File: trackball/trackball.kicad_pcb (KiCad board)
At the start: 2 copper layers, 15 x 13.1 mm, 13 parts, among them P8 CONN_7, U1 BU52012HFV-TR, U2 BU52012HFV-TR, U3 BU52012HFV-TR, U4 BU52012HFV-TR

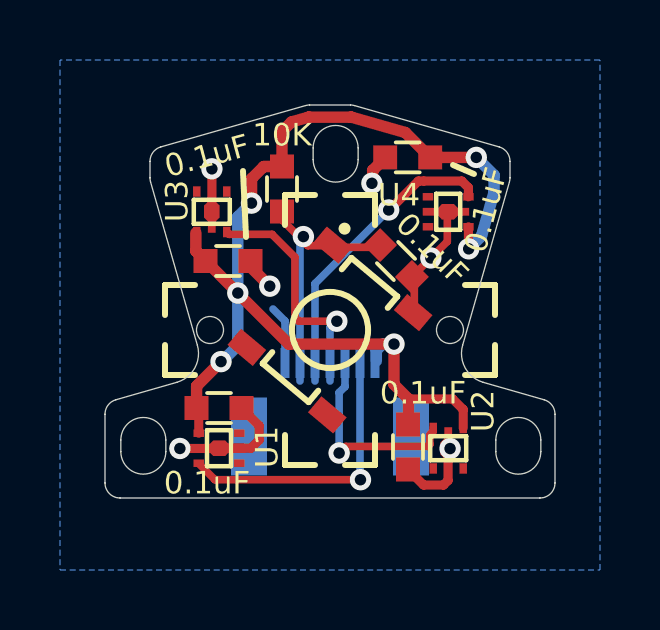
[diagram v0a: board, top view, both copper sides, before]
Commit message: Resolve 1 DRC error. 2 to go.
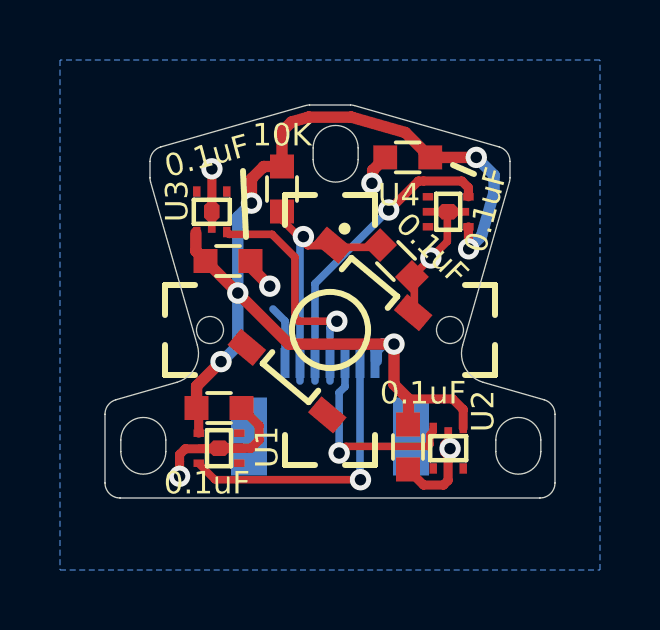
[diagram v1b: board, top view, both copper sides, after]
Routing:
- net GND: track 17.3 -> 18.1 mm
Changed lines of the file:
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@@
     (thickness 1.6)
     (drawings 43)
-    (tracks 128)
+    (tracks 131)
     (zones 0)
     (modules 13)
@@
     (effects (font (size 0.75 0.75) (thickness 0.15)) (justify mirror))
   )
-  (via (at 194.9958 153.9494) (size 0.7112) (drill 0.381) (layers F.Cu B.Cu) (net 1))
   (segment (start 202.810749 148.310749) (end 202.73033 148.23033) (width 0.254) (layer F.Cu) (net 1))
   (segment (start 202.810749 149.664124) (end 202.810749 148.310749) (width 0.254) (layer F.Cu) (net 1))
@@
   (segment (start 197.11 153.94) (end 196.0974 153.94) (width 0.3048) (layer F.Cu) (net 1))
   (segment (start 196.0974 153.94) (end 196.088 153.9306) (width 0.3048) (layer F.Cu) (net 1))
-  (segment (start 196.2906 153.9494) (end 196.3 153.94) (width 0.3048) (layer F.Cu) (net 1))
-  (segment (start 194.9958 153.9494) (end 196.2906 153.9494) (width 0.3048) (layer F.Cu) (net 1))
   (segment (start 197.6374 153.1874) (end 197.05 152.6) (width 0.3048) (layer F.Cu) (net 1))
   (segment (start 197.6374 153.67) (end 197.6374 153.1874) (width 0.3048) (layer F.Cu) (net 1))
@@
   (segment (start 201.8404 144.26) (end 201.422 144.6784) (width 0.381) (layer F.Cu) (net 1))
   (via (at 204.002044 153.951866) (size 0.7112) (drill 0.381) (layers F.Cu B.Cu) (net 1))
+  (via (at 194.986061 154.876501) (size 0.7112) (drill 0.381) (layers F.Cu B.Cu) (net 1))
+  (segment (start 196.3 153.94) (end 196.280601 153.959399) (width 0.3048) (layer F.Cu) (net 1))
+  (segment (start 196.280601 153.959399) (end 195.178044 153.959399) (width 0.3048) (layer F.Cu) (net 1))
+  (segment (start 195.178044 153.959399) (end 194.986061 154.151382) (width 0.3048) (layer F.Cu) (net 1))
+  (segment (start 194.986061 154.373607) (end 194.986061 154.876501) (width 0.3048) (layer F.Cu) (net 1))
+  (segment (start 194.986061 154.151382) (end 194.986061 154.373607) (width 0.3048) (layer F.Cu) (net 1))
   (segment (start 200.390425 147.2438) (end 200.335876 147.189251) (width 0.254) (layer F.Cu) (net 2))
   (segment (start 201.66967 147.16967) (end 201.59554 147.2438) (width 0.254) (layer F.Cu) (net 2))

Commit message: Move top edge upward by 0.3 mm. Resolve DRC issues.
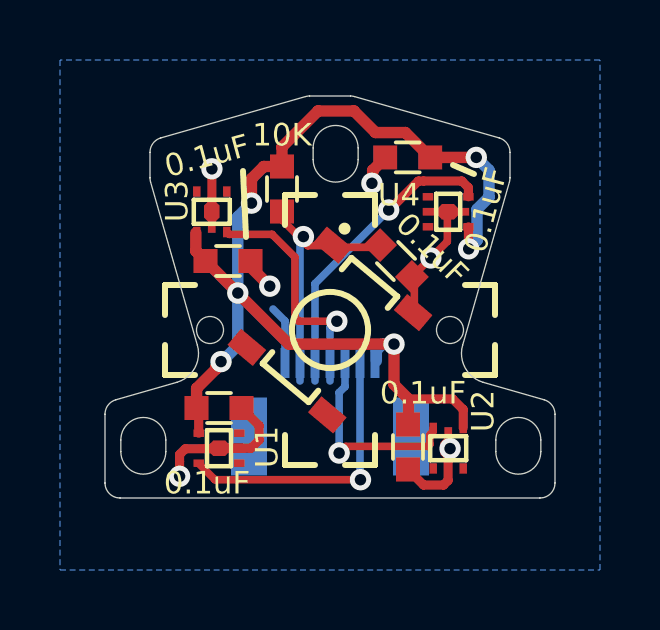
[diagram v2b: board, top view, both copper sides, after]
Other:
- board size 15 x 13.1 mm -> 15 x 13.4 mm
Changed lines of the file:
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@@
     (thickness 1.6)
     (drawings 43)
-    (tracks 131)
+    (tracks 132)
     (zones 0)
     (modules 13)
@@
   )
   (setup
-    (last_trace_width 0.2032)
+    (last_trace_width 0.381)
     (user_trace_width 0.2032)
     (user_trace_width 0.254)
@@
   (gr_circle (center 203.94 153.94) (end 203.99 153.94) (layer Eco2.User) (width 0.1))
   (gr_circle (center 196.06 146.06) (end 196.11 146.06) (layer Eco2.User) (width 0.1))
-  (gr_arc (start 199.320057 143.000091) (end 199.32003 142.499997) (angle -15.6) (layer Edge.Cuts) (width 0.01))
-  (gr_arc (start 200.679943 143.000091) (end 200.817329 142.519238) (angle -15.7) (layer Edge.Cuts) (width 0.01))
+  (gr_arc (start 199.320057 142.700091) (end 199.32003 142.199997) (angle -15.6) (layer Edge.Cuts) (width 0.01))
+  (gr_arc (start 200.679943 142.700091) (end 200.817329 142.219238) (angle -15.7) (layer Edge.Cuts) (width 0.01))
   (gr_arc (start 193.000061 155.099935) (end 192.5 155.100003) (angle -89.9) (layer Edge.Cuts) (width 0.01))
-  (gr_arc (start 194.500041 144.377192) (end 194.36264 143.89639) (angle -74) (layer Edge.Cuts) (width 0.01))
-  (gr_arc (start 205.499959 144.377192) (end 206 144.377148) (angle -74) (layer Edge.Cuts) (width 0.01))
+  (gr_arc (start 194.500041 144.077192) (end 194.36264 143.59639) (angle -74) (layer Edge.Cuts) (width 0.01))
+  (gr_arc (start 205.499959 144.077192) (end 206 144.077148) (angle -74) (layer Edge.Cuts) (width 0.01))
   (gr_arc (start 206.999958 152.806915) (end 207.5 152.806897) (angle -74) (layer Edge.Cuts) (width 0.01))
   (gr_arc (start 206.999932 155.099935) (end 207 155.600003) (angle -89.9) (layer Edge.Cuts) (width 0.01))
@@
   (gr_line (start 192.862183 152.32626) (end 194.893456 151.743802) (angle 90) (layer Edge.Cuts) (width 0.01))
   (gr_line (start 195.579079 150.506909) (end 194.019371 145.067548) (angle 90) (layer Edge.Cuts) (width 0.01))
-  (gr_line (start 200.817329 142.519238) (end 205.63736 143.89639) (angle 90) (layer Edge.Cuts) (width 0.01))
-  (gr_line (start 194.36264 143.89639) (end 199.182671 142.519238) (angle 90) (layer Edge.Cuts) (width 0.01))
-  (gr_line (start 194 144.92973) (end 194 144.377148) (angle 90) (layer Edge.Cuts) (width 0.01))
+  (gr_line (start 200.817329 142.219238) (end 205.63736 143.59639) (angle 90) (layer Edge.Cuts) (width 0.01))
+  (gr_line (start 194.36264 143.59639) (end 199.182671 142.219238) (angle 90) (layer Edge.Cuts) (width 0.01))
+  (gr_line (start 194 144.92973) (end 194 144.077148) (angle 90) (layer Edge.Cuts) (width 0.01))
   (gr_line (start 205.106544 151.743802) (end 207.137817 152.32626) (angle 90) (layer Edge.Cuts) (width 0.01))
-  (gr_line (start 199.32003 142.499997) (end 200.67997 142.499997) (angle 90) (layer Edge.Cuts) (width 0.01))
-  (gr_line (start 206 144.377148) (end 206 144.92973) (angle 90) (layer Edge.Cuts) (width 0.01))
+  (gr_line (start 199.32003 142.199997) (end 200.67997 142.199997) (angle 90) (layer Edge.Cuts) (width 0.01))
+  (gr_line (start 206 144.077148) (end 206 144.92973) (angle 90) (layer Edge.Cuts) (width 0.01))
   (gr_line (start 205.980629 145.067548) (end 204.420921 150.506909) (angle 90) (layer Edge.Cuts) (width 0.01))
   (gr_line (start 205.52729 154.054501) (end 205.52729 153.665707) (angle 90) (layer Edge.Cuts) (width 0.01))
@@
   (segment (start 195.5546 152.5016) (end 195.5546 152.6286) (width 0.381) (layer F.Cu) (net 4))
   (via (at 196.3674 151.0538) (size 0.7112) (drill 0.381) (layers F.Cu B.Cu) (net 4))
-  (segment (start 195.5546 152.5778) (end 195.5546 151.8666) (width 0.381) (layer F.Cu) (net 4))
-  (segment (start 195.5546 151.8666) (end 196.3674 151.0538) (width 0.381) (layer F.Cu) (net 4))
   (segment (start 196.9262 148.9964) (end 196.9262 150.5204) (width 0.381) (layer B.Cu) (net 4))
   (segment (start 196.9262 150.5204) (end 196.3928 151.0538) (width 0.381) (layer B.Cu) (net 4))
@@
   (via (at 204.8764 144.2466) (size 0.7112) (drill 0.381) (layers F.Cu B.Cu) (net 4))
   (segment (start 203.3404 144.2466) (end 204.8764 144.2466) (width 0.381) (layer F.Cu) (net 4))
-  (segment (start 200.734074 142.910116) (end 202.511853 143.418053) (width 0.381) (layer F.Cu) (net 4))
-  (segment (start 198.4 144.55) (end 198.4 143.3824) (width 0.381) (layer F.Cu) (net 4))
-  (segment (start 198.4 143.3824) (end 198.714828 143.067572) (width 0.381) (layer F.Cu) (net 4))
-  (segment (start 198.714828 143.067572) (end 199.267735 142.909598) (width 0.381) (layer F.Cu) (net 4))
-  (segment (start 199.267735 142.909598) (end 199.300098 142.905164) (width 0.381) (layer F.Cu) (net 4))
-  (segment (start 199.300098 142.905164) (end 200.699292 142.905164) (width 0.381) (layer F.Cu) (net 4))
-  (segment (start 202.511853 143.418053) (end 203.3404 144.2466) (width 0.381) (layer F.Cu) (net 4))
-  (segment (start 200.699292 142.905164) (end 200.734074 142.910116) (width 0.381) (layer F.Cu) (net 4))
-  (segment (start 205.468713 145.406312) (end 205.049815 146.867185) (width 0.381) (layer B.Cu) (net 4))
-  (segment (start 205.049815 146.867185) (end 204.6224 147.2946) (width 0.381) (layer B.Cu) (net 4))
-  (segment (start 205.468713 144.838913) (end 205.468713 145.406312) (width 0.381) (layer B.Cu) (net 4))
-  (segment (start 204.8764 144.2466) (end 205.468713 144.838913) (width 0.381) (layer B.Cu) (net 4))
   (via (at 204.6224 147.2946) (size 0.7112) (drill 0.381) (layers F.Cu B.Cu) (net 4))
   (segment (start 204.615 147.2872) (end 204.6224 147.2946) (width 0.3048) (layer F.Cu) (net 4))
@@
   (segment (start 195.625 152.675) (end 195.55 152.6) (width 0.3048) (layer F.Cu) (net 4))
   (segment (start 195.625 153.44) (end 195.625 152.675) (width 0.3048) (layer F.Cu) (net 4))
+  (segment (start 198.4 143.9) (end 198.4 144.5) (width 0.381) (layer F.Cu) (net 4))
+  (segment (start 199.6 142.7) (end 198.4 143.9) (width 0.381) (layer F.Cu) (net 4))
+  (segment (start 200.8 142.7) (end 199.6 142.7) (width 0.381) (layer F.Cu) (net 4))
+  (segment (start 203.3404 144.2466) (end 202.511853 143.418053) (width 0.381) (layer F.Cu) (net 4))
+  (segment (start 201.518053 143.418053) (end 200.8 142.7) (width 0.381) (layer F.Cu) (net 4))
+  (segment (start 202.511853 143.418053) (end 201.518053 143.418053) (width 0.381) (layer F.Cu) (net 4))
+  (segment (start 204.9 147.017) (end 204.6224 147.2946) (width 0.381) (layer B.Cu) (net 4))
+  (segment (start 204.9 145.975025) (end 204.9 147.017) (width 0.381) (layer B.Cu) (net 4))
+  (segment (start 205.3 145.575025) (end 204.9 145.975025) (width 0.381) (layer B.Cu) (net 4))
+  (segment (start 204.8764 144.2466) (end 205.3 144.6702) (width 0.381) (layer B.Cu) (net 4))
+  (segment (start 205.3 144.6702) (end 205.3 145.575025) (width 0.381) (layer B.Cu) (net 4))
+  (segment (start 196.2 151.2212) (end 196.3674 151.0538) (width 0.381) (layer F.Cu) (net 4))
+  (segment (start 196.2 151.3) (end 196.2 151.2212) (width 0.381) (layer F.Cu) (net 4))
+  (segment (start 195.5546 152.5778) (end 195.5546 151.9454) (width 0.381) (layer F.Cu) (net 4))
+  (segment (start 195.5546 151.9454) (end 196.2 151.3) (width 0.381) (layer F.Cu) (net 4))
   (via (at 200.3044 154.1018) (size 0.7112) (drill 0.381) (layers F.Cu B.Cu) (net 5))
   (segment (start 200.3044 152.083608) (end 200.3044 154.1018) (width 0.254) (layer B.Cu) (net 5))

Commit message: Move FFC connector upwards by 2 mm.
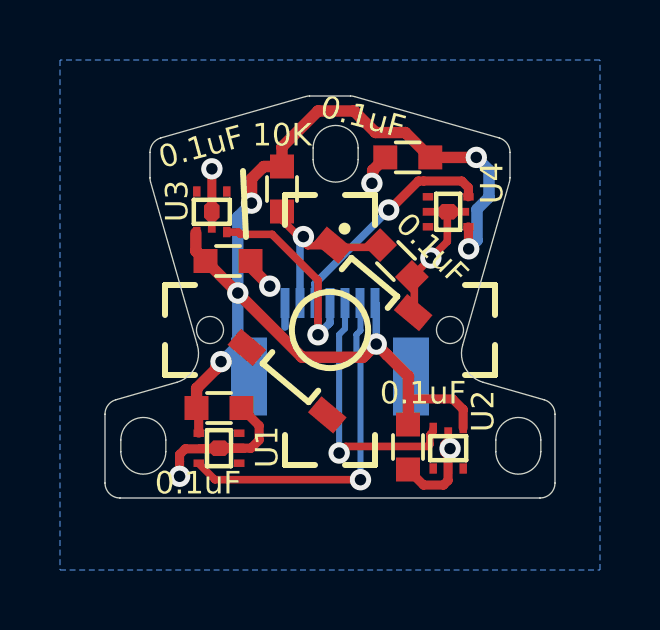
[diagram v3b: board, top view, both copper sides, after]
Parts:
- moved P8 2.00 mm to (200.0, 153.1)
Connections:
- P8 pad : (no net) -> GND
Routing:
- net /TB_RIGHT: track 10.1 -> 7.51 mm
- net /TB_BTN: track 9.23 -> 6.82 mm
- net /TB_DOWN: track 6.82 -> 8.92 mm
- net /TB_LEFT: track 9.50 -> 11.5 mm
- net /TB_UP: track 8.19 -> 6.75 mm
- net GND: track 18.1 -> 17.1 mm

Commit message: Fix the angle of C5.
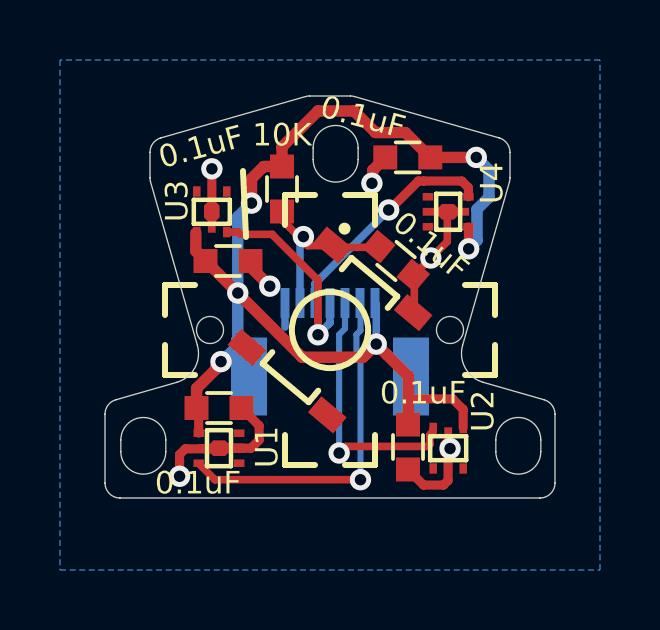
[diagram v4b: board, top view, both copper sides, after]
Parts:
- turned C5 to 140 degrees
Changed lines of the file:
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@@
     (at 200 153.1 180)
     (attr smd)
-    (fp_text reference P8 (at 2.5 4.2 180) (layer B.SilkS)
+    (fp_text reference P8 (at -2.5 4.2 180) (layer B.SilkS)
       (effects (font (size 0.75 0.75) (thickness 0.15)) (justify mirror))
     )
@@
   )
   (module UGL:SM0603 (layer F.Cu)
-    (at 202.2 147.7 135)
-    (attr smd)
-    (fp_text reference C5 (at 0 0 135) (layer B.SilkS)
-      (effects (font (size 0.75 0.75) (thickness 0.15)) (justify mirror))
-    )
-    (fp_text value 0.1uF (at -0.565685 1.131371 135) (layer F.SilkS)
-      (effects (font (size 0.75 0.75) (thickness 0.15)))
-    )
-    (fp_line (start -0.4 -0.5) (end 0.4 -0.5) (layer F.SilkS) (width 0.127))
-    (fp_line (start 0.4 0.5) (end -0.4 0.5) (layer F.SilkS) (width 0.127))
-    (pad 1 smd rect (at -0.75 0 135) (size 0.8 0.8) (layers F.Cu F.Paste F.Mask)
-      (net 1 GND))
-    (pad 2 smd rect (at 0.75 0 135) (size 0.8 0.8) (layers F.Cu F.Paste F.Mask)
+    (at 202.2 147.7 140)
+    (attr smd)
+    (fp_text reference C5 (at 0 0 140) (layer B.SilkS)
+      (effects (font (size 0.75 0.75) (thickness 0.15)) (justify mirror))
+    )
+    (fp_text value 0.1uF (at -0.565685 1.131371 140) (layer F.SilkS)
+      (effects (font (size 0.75 0.75) (thickness 0.15)))
+    )
+    (fp_line (start -0.4 -0.5) (end 0.4 -0.5) (layer F.SilkS) (width 0.127))
+    (fp_line (start 0.4 0.5) (end -0.4 0.5) (layer F.SilkS) (width 0.127))
+    (pad 1 smd rect (at -0.75 0 140) (size 0.8 0.8) (layers F.Cu F.Paste F.Mask)
+      (net 1 GND))
+    (pad 2 smd rect (at 0.75 0 140) (size 0.8 0.8) (layers F.Cu F.Paste F.Mask)
       (net 2 /TB_BTN))
     (model smd\resistors\R0603.wrl
@@
   (module UGL:TL3315NF250Q (layer F.Cu)
     (at 200 150 50)
-    (fp_text reference BTN1 (at 0.842649 -0.707066 180) (layer B.SilkS)
-      (effects (font (size 0.746 0.746) (thickness 0.15)) (justify mirror))
+    (fp_text reference BTN1 (at 1.608693 -1.349854 180) (layer B.SilkS)
+      (effects (font (size 0.75 0.75) (thickness 0.15)) (justify mirror))
     )
     (fp_text value BTN (at 0 3.1 50) (layer Eco1.User) hide
